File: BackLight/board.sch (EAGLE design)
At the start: 16 parts

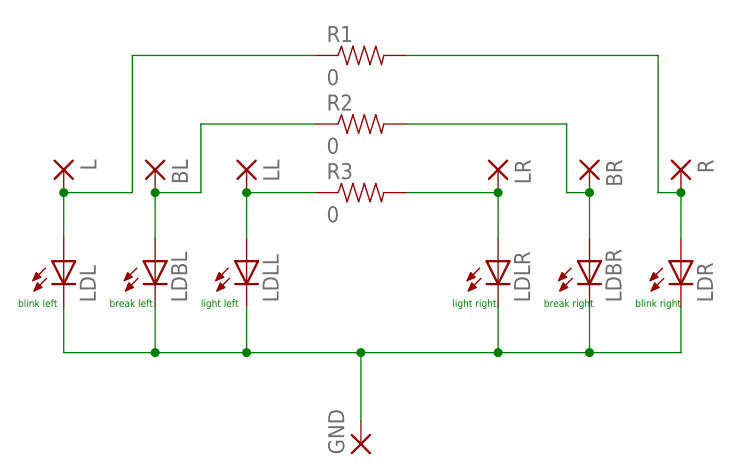
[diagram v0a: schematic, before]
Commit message: Fix light board. Fix carsystem board.
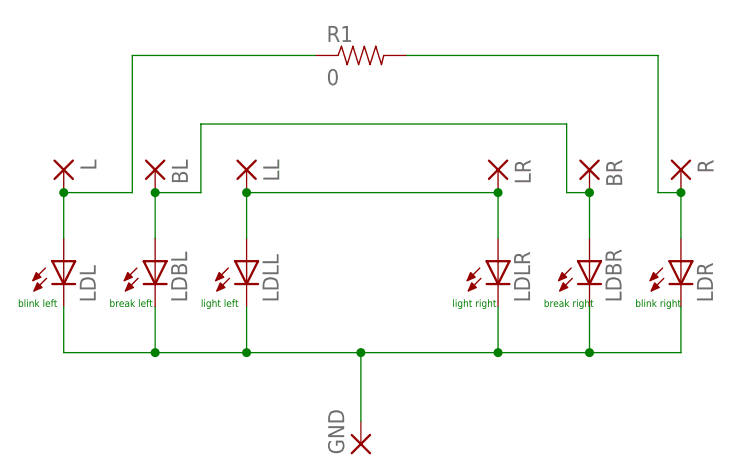
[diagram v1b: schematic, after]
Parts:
- removed R2, R3: 0, SparkFun-Resistors:1.5KOHM-1/10W-1%(0603)
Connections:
- removed net N$5: LDLR.A, LR.P, R3.2
- removed net N$6: BR.P, LDBR.A, R2.2
- net N$3: now also BR.P, LDBR.A; no longer R2.1
- net N$4: now also LDLR.A, LR.P; no longer R3.1
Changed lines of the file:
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@@
 <part name="R" library="wirepad" deviceset="SMD2" device=""/>
 <part name="R1" library="SparkFun-Resistors" deviceset="1.5KOHM-1/10W-1%(0603)" device="" value="0"/>
-<part name="R2" library="SparkFun-Resistors" deviceset="1.5KOHM-1/10W-1%(0603)" device="" value="0"/>
-<part name="R3" library="SparkFun-Resistors" deviceset="1.5KOHM-1/10W-1%(0603)" device="" value="0"/>
 </parts>
 <sheets>
@@
 <instance part="R" gate="1" x="71.12" y="81.28" rot="R270"/>
 <instance part="R1" gate="G$1" x="35.56" y="93.98"/>
-<instance part="R2" gate="G$1" x="35.56" y="86.36"/>
-<instance part="R3" gate="G$1" x="35.56" y="78.74"/>
 </instances>
 <busses>
@@
 <wire x1="17.78" y1="78.74" x2="17.78" y2="86.36" width="0.1524" layer="91"/>
 <junction x="12.7" y="78.74"/>
-<pinref part="R2" gate="G$1" pin="1"/>
-<wire x1="17.78" y1="86.36" x2="30.48" y2="86.36" width="0.1524" layer="91"/>
+<wire x1="17.78" y1="86.36" x2="58.42" y2="86.36" width="0.1524" layer="91"/>
+<pinref part="BR" gate="1" pin="P"/>
+<pinref part="LDBR" gate="G$1" pin="A"/>
+<wire x1="60.96" y1="78.74" x2="60.96" y2="73.66" width="0.1524" layer="91"/>
+<wire x1="58.42" y1="86.36" x2="58.42" y2="78.74" width="0.1524" layer="91"/>
+<wire x1="58.42" y1="78.74" x2="60.96" y2="78.74" width="0.1524" layer="91"/>
+<junction x="60.96" y="78.74"/>
 </segment>
 </net>
@@
 <pinref part="LDLL" gate="G$1" pin="A"/>
 <wire x1="22.86" y1="78.74" x2="22.86" y2="73.66" width="0.1524" layer="91"/>
-<pinref part="R3" gate="G$1" pin="1"/>
-<wire x1="22.86" y1="78.74" x2="30.48" y2="78.74" width="0.1524" layer="91"/>
 <junction x="22.86" y="78.74"/>
-</segment>
-</net>
-<net name="N$5" class="0">
-<segment>
 <pinref part="LR" gate="1" pin="P"/>
 <pinref part="LDLR" gate="G$1" pin="A"/>
 <wire x1="50.8" y1="78.74" x2="50.8" y2="73.66" width="0.1524" layer="91"/>
-<pinref part="R3" gate="G$1" pin="2"/>
-<wire x1="40.64" y1="78.74" x2="50.8" y2="78.74" width="0.1524" layer="91"/>
 <junction x="50.8" y="78.74"/>
+<wire x1="22.86" y1="78.74" x2="50.8" y2="78.74" width="0.1524" layer="91"/>
 </segment>
 </net>
-<net name="N$6" class="0">
-<segment>
-<pinref part="BR" gate="1" pin="P"/>
-<pinref part="LDBR" gate="G$1" pin="A"/>
-<wire x1="60.96" y1="78.74" x2="60.96" y2="73.66" width="0.1524" layer="91"/>
-<pinref part="R2" gate="G$1" pin="2"/>
-<wire x1="40.64" y1="86.36" x2="58.42" y2="86.36" width="0.1524" layer="91"/>
-<wire x1="58.42" y1="86.36" x2="58.42" y2="78.74" width="0.1524" layer="91"/>
-<wire x1="58.42" y1="78.74" x2="60.96" y2="78.74" width="0.1524" layer="91"/>
-<junction x="60.96" y="78.74"/>
-</segment>
-</net>
